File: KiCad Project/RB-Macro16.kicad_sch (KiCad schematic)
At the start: 65 parts, among them J1 USB_C_Receptacle, K0A1 KEYSW, K0B1 KEYSW, K0C1 KEYSW, K0D1 KEYSW, K1A1 KEYSW, K1B1 KEYSW, K1C1 KEYSW, K1D1 KEYSW, K2A1 KEYSW, K2B1 KEYSW, K2C1 KEYSW, K2D1 KEYSW, K3A1 KEYSW, K3B1 KEYSW, K3C1 KEYSW, K3D1 KEYSW, SW1 SW_PUSH, U1 ATMEGA32U4, X1 XTAL_GND

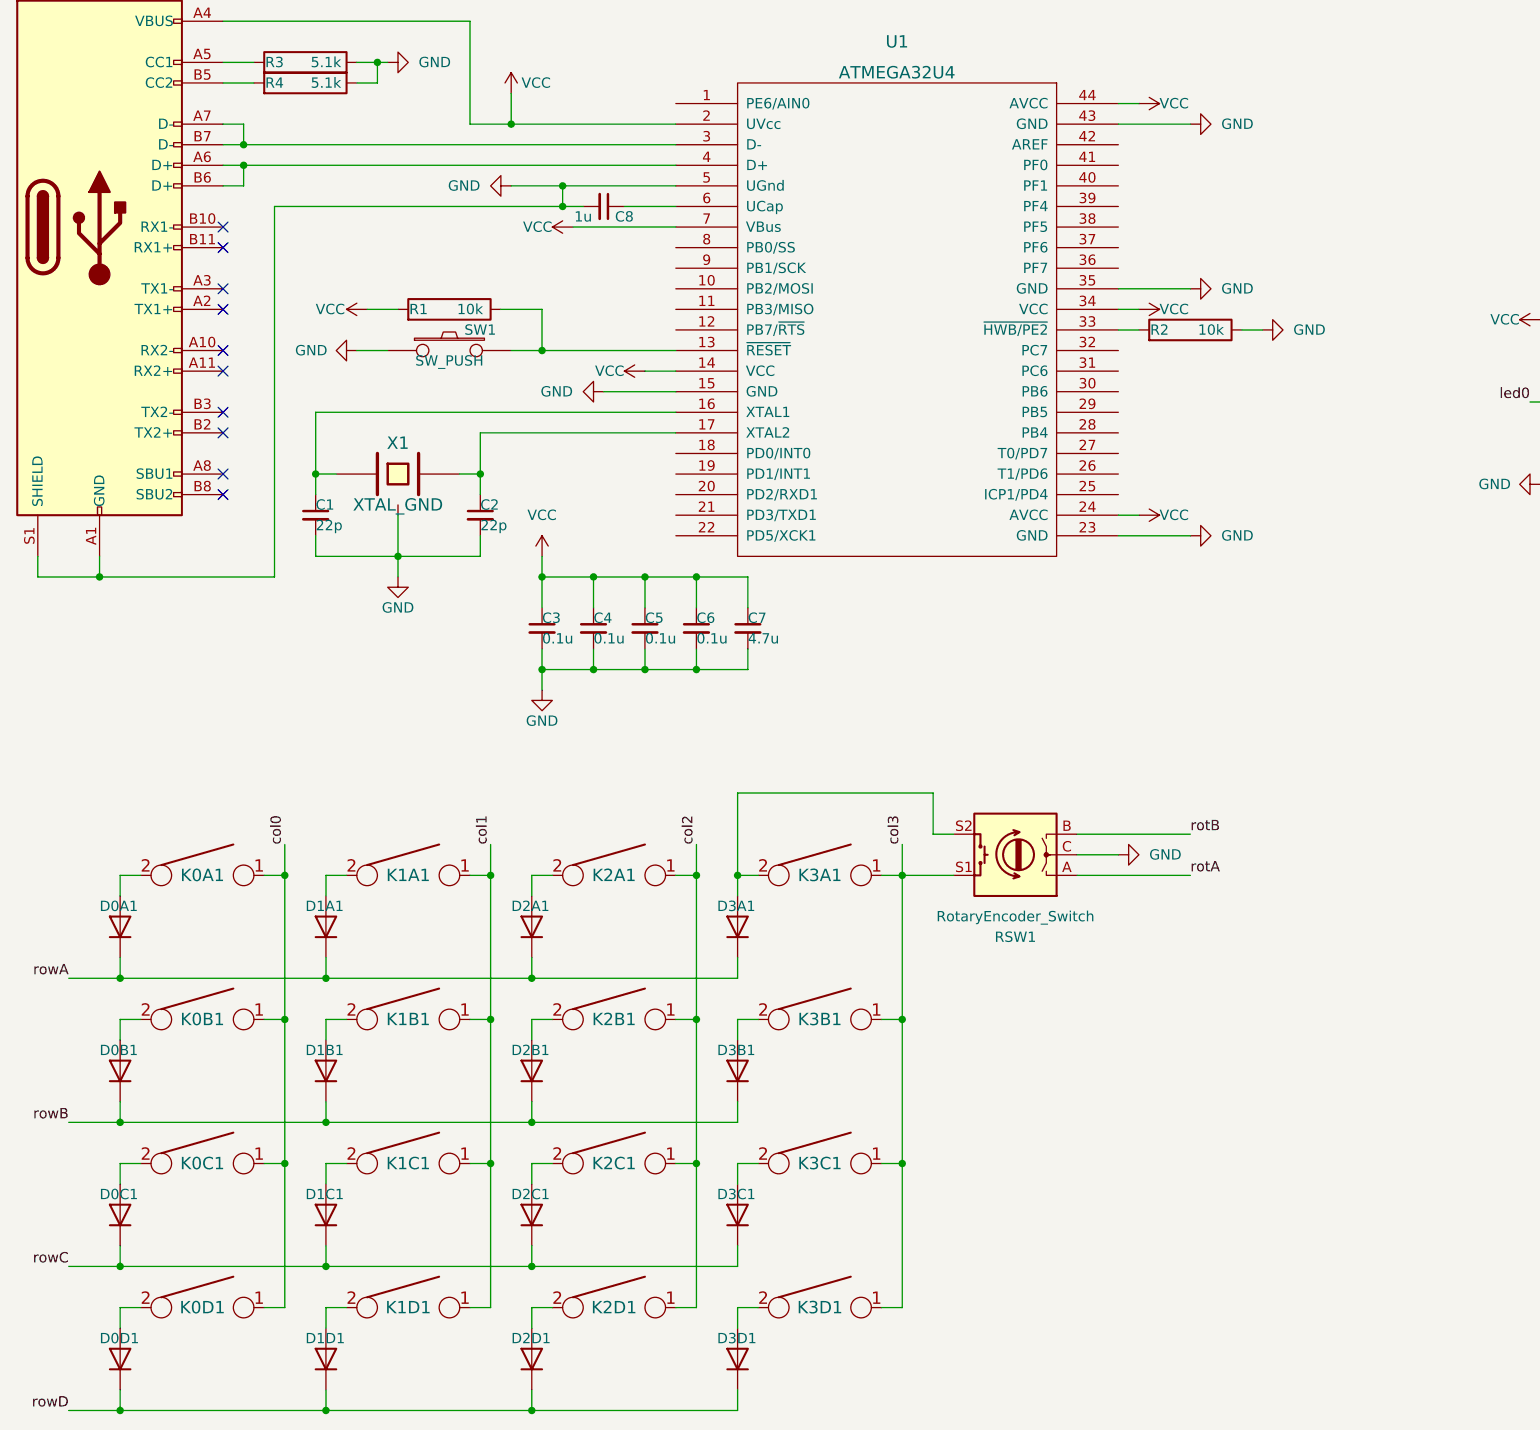
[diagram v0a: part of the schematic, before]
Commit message: Finished Schematic
Finished the schematic and associated all footprints to prep for PCB design
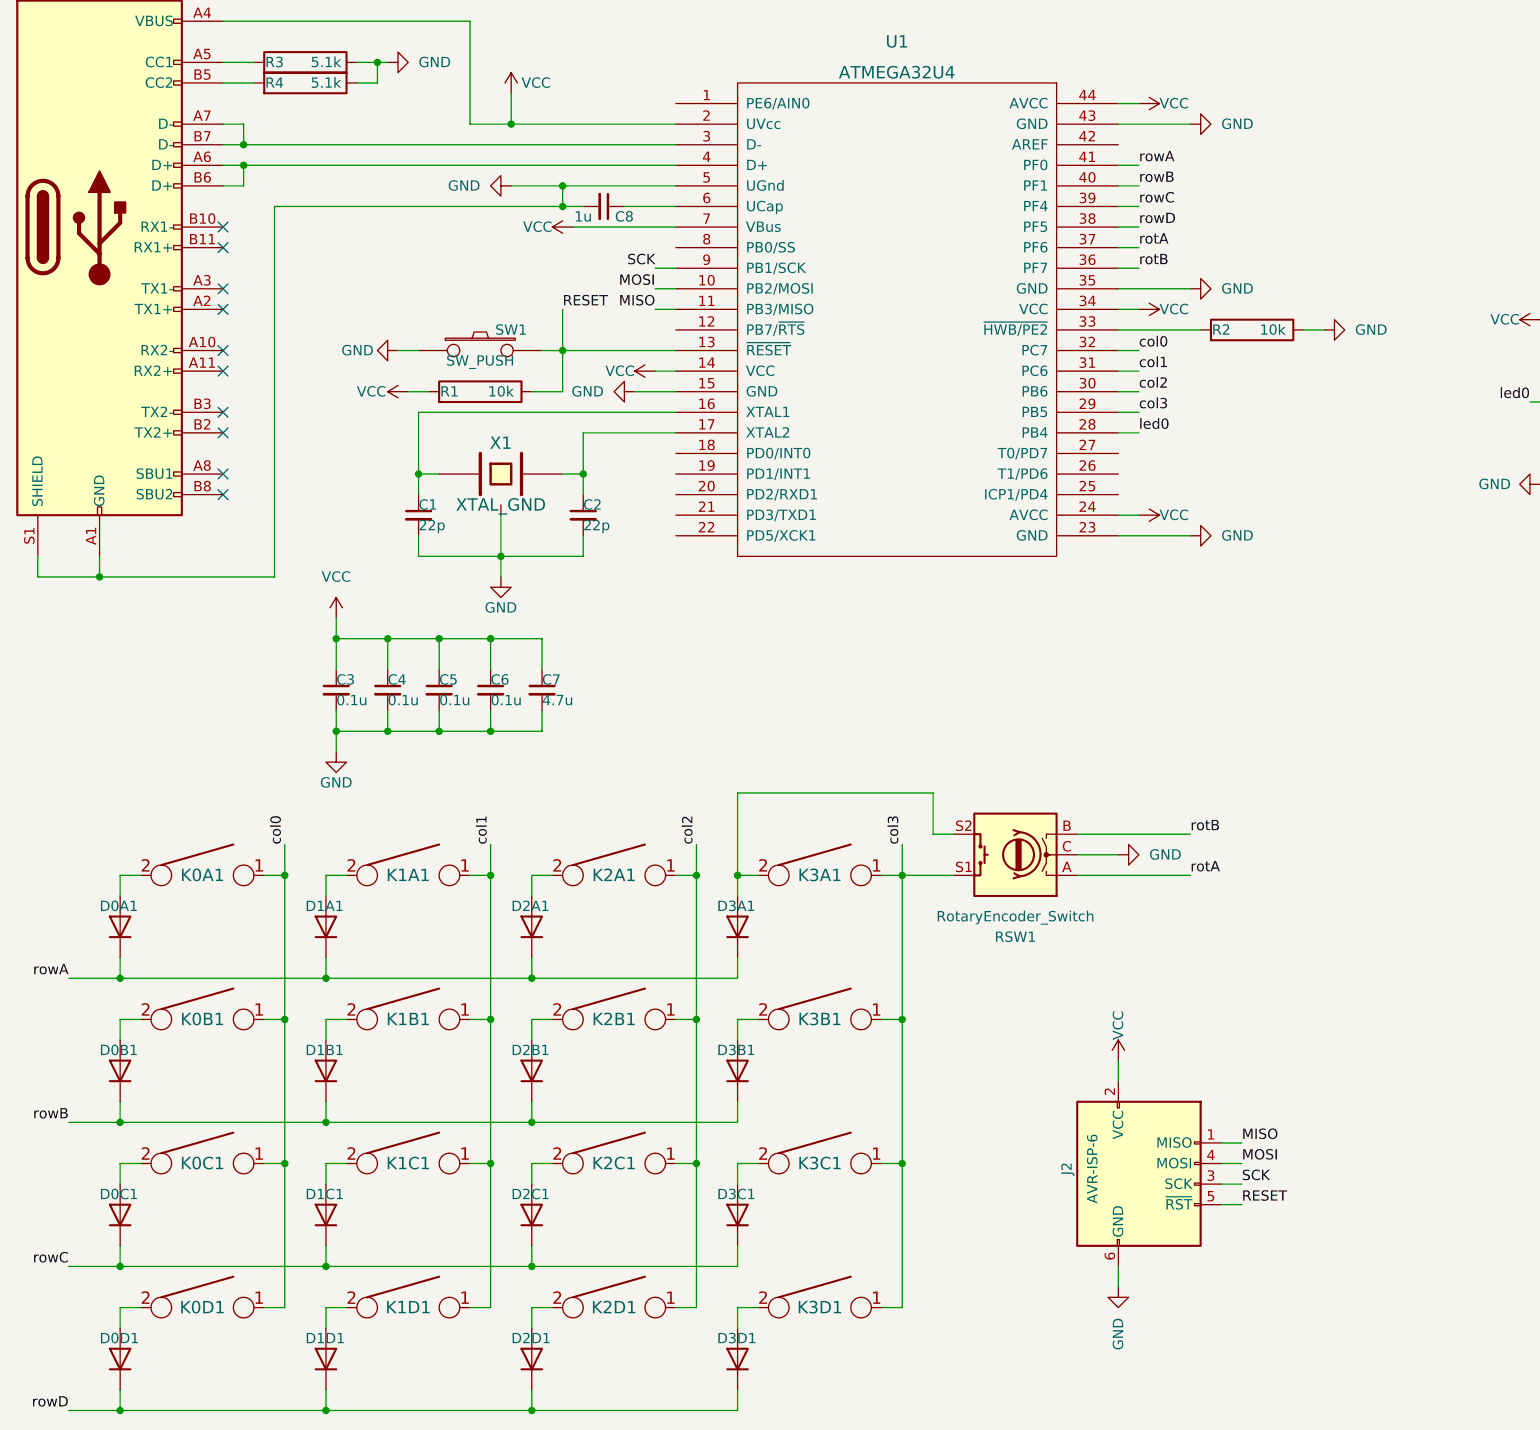
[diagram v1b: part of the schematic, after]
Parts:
- added J2: AVR-ISP-6, keyboard_parts.pretty-master:AVR_ICSP_3x2, symbol Connector:AVR-ISP-6
- C1, C2, C3, C4, C5, C6, C7, C8: footprint (none) -> Capacitor_SMD:C_0805_2012Metric_Pad1.18x1.45mm_HandSolder
- D0A1, D0B1, D0C1, D0D1, D1A1, D1B1, D1C1, D1D1, D2A1, D2B1, D2C1, D2D1, D3A1, D3B1, D3C1, D3D1: footprint (none) -> Diode_THT:D_DO-35_SOD27_P7.62mm_Horizontal
- J1: footprint (none) -> Connector_USB:USB_C_Receptacle_Amphenol_12401610E4-2A
- K0A1, K0B1, K0C1, K0D1, K1A1, K1B1, K1C1, K1D1, K2A1, K2B1, K2C1, K2D1, K3A1, K3B1, K3C1, K3D1: footprint (none) -> keyswitches.pretty-master:Kailh_socket_MX
- R1, R2, R3, R4: footprint (none) -> Resistor_THT:R_Axial_DIN0207_L6.3mm_D2.5mm_P7.62mm_Horizontal
- RSW1: footprint (none) -> Rotary_Encoder:RotaryEncoder_Alps_EC12E_Vertical_H20mm
- SW1: footprint (none) -> Button_Switch_THT:SW_PUSH_6mm
- U1: footprint (none) -> Package_QFP:TQFP-44_10x10mm_P0.8mm
- X1: footprint (none) -> Crystal:Crystal_SMD_SeikoEpson_FA238-4Pin_3.2x2.5mm_HandSoldering
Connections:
- net GND: now also J2.6 (GND)
- net VCC: now also J2.2 (VCC)
- net col0: now also U1.32 (PC7)
- net col1: now also U1.31 (PC6)
- net col2: now also U1.30 (PB6)
- net col3: now also U1.29 (PB5)
- net led0: now also U1.28 (PB4)
- net rotA: now also U1.37 (PF6)
- net rotB: now also U1.36 (PF7)
- net rowA: now also U1.41 (PF0)
- net rowB: now also U1.40 (PF1)
- net rowC: now also U1.39 (PF4)
- net rowD: now also U1.38 (PF5)
- net RESET: now reaches R1.2, SW1.2, U1.13 (~{RESET})
- net RESET: now also J2.5 (~{RST})
- net MOSI: now reaches U1.10 (PB2/MOSI)
- net MOSI: now also J2.4 (MOSI)
- net MISO: now reaches U1.11 (PB3/MISO)
- net MISO: now also J2.1 (MISO)
- net SCK: now reaches U1.9 (PB1/SCK)
- net SCK: now also J2.3 (SCK)
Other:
- moved on the sheet: C1, C2, C3, C4, C5, C6, C7, R1, R2, SW1, X1

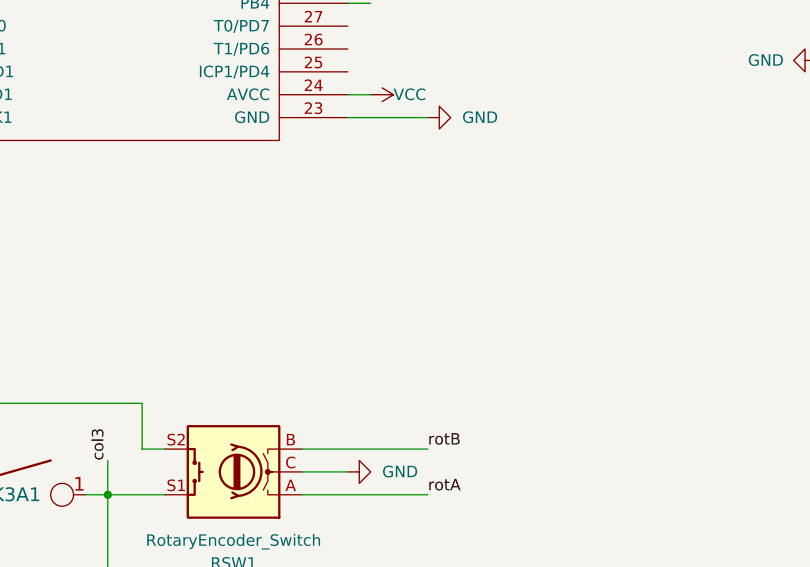
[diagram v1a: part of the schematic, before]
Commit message: New Switch Found
Found a new MX Switch with LITEON LEDs
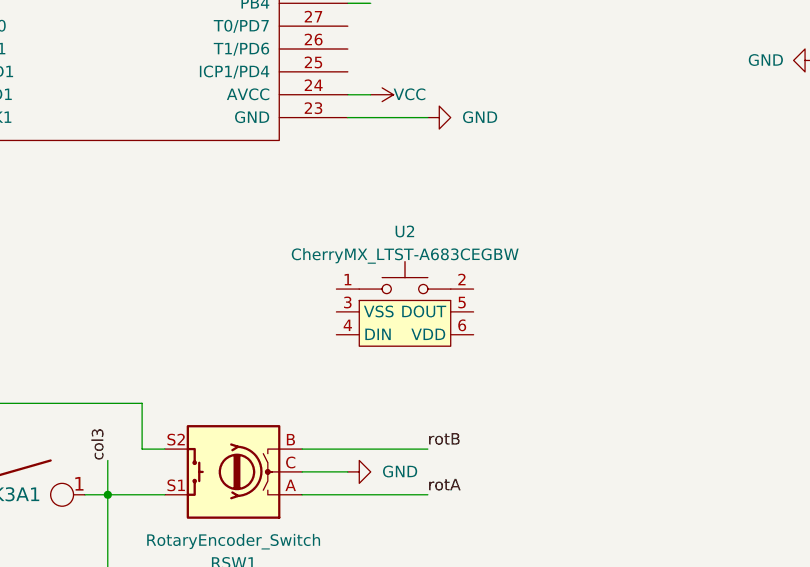
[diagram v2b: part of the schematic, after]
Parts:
- added U2: CherryMX_LTST-A683CEGBW, CherryMX_KailhSocket_LTST-A683CEGBW:CherryMX_1.00u_KailhSocket_LTST-A683CEGBW, symbol CherryMX:CherryMX_LTST-A683CEGBW
- J2: footprint keyboard_parts.pretty-master:AVR_ICSP_3x2 -> keyboard_parts:AVR_ICSP_3x2
- K0A1, K0B1, K0C1, K0D1, K1A1, K1B1, K1C1, K1D1, K2A1, K2B1, K2C1, K2D1, K3A1, K3B1, K3C1, K3D1: footprint keyswitches.pretty-master:Kailh_socket_MX -> CherryMX_KailhSocket_LED:CherryMX_1.00u_KailhSocket_LED
- LED0A1, LED0B1, LED0C1, LED0D1, LED1A1, LED1B1, LED1C1, LED1D1, LED2A1, LED2B1, LED2C1, LED2D1, LED3A1, LED3B1, LED3C1, LED3D1: footprint LED_SMD:LED_SK6812_PLCC4_5.0x5.0mm_P3.2mm -> LED_SMD:LED_SK6812_EC15_1.5x1.5mm
